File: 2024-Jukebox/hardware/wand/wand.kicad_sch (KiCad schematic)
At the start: 48 parts, among them J1 USB_C_Receptacle_USB2.0, J2 Conn_01x05, J3 Conn_01x04, J4 Conn_01x04, J5 Conn_01x04, J6 Conn_01x01, J7 Conn_01x04, Q1 MUN5214DW1T1G, Q2 BSS138, Q3 CJ3139K, Q5 BSS138, SW1 SW_SPDT, U1 CP2104, U2 ESP32-PICO-D4, U3 ICM-20948, U4 TP4065-4.2V, U5 MIC5225-3.3, U6 LY68L6400SLIT, U7 MIC5225-1.8

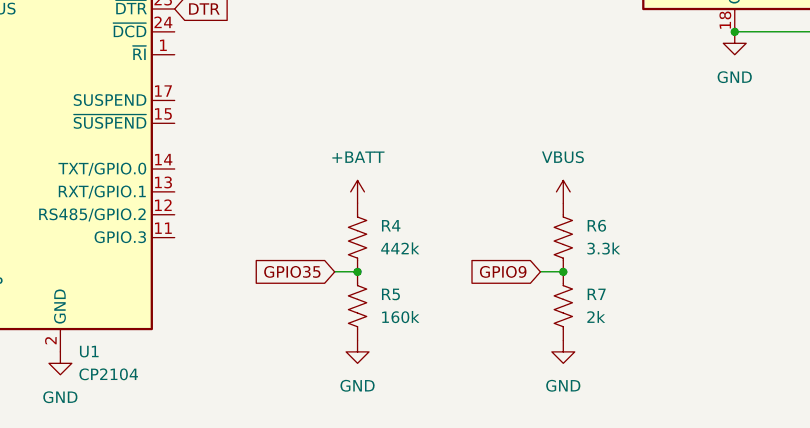
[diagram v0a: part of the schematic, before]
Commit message: Added wand production files
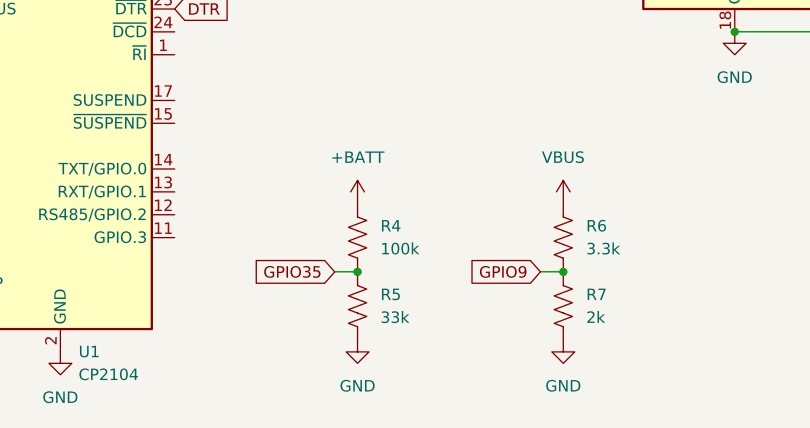
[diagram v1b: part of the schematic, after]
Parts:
- R4: value 442k -> 100k
- R5: value 160k -> 33k
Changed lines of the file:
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@@
       (effects (font (size 1.27 1.27)) (justify left))
     )
-    (property "Value" "160k" (at 125.73 180.34 0)
+    (property "Value" "33k" (at 125.73 180.34 0)
       (effects (font (size 1.27 1.27)) (justify left))
     )
@@
       (effects (font (size 1.27 1.27)) (justify left))
     )
-    (property "Value" "442k" (at 125.73 172.72 0)
-      (effects (font (size 1.27 1.27)) (justify left))
-    )
+    (property "Value" "100k" (at 125.73 172.72 0)
+      (effects (font (size 1.27 1.27)) (justify left))
+    )

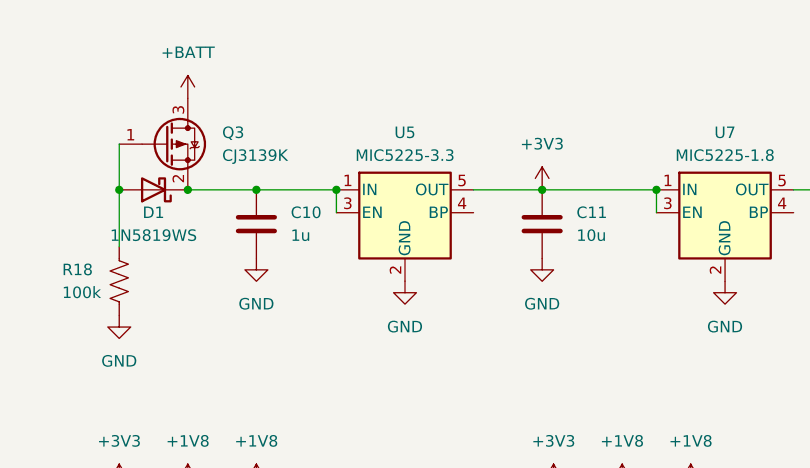
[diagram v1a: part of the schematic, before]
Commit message: Changed 3.3v regulator
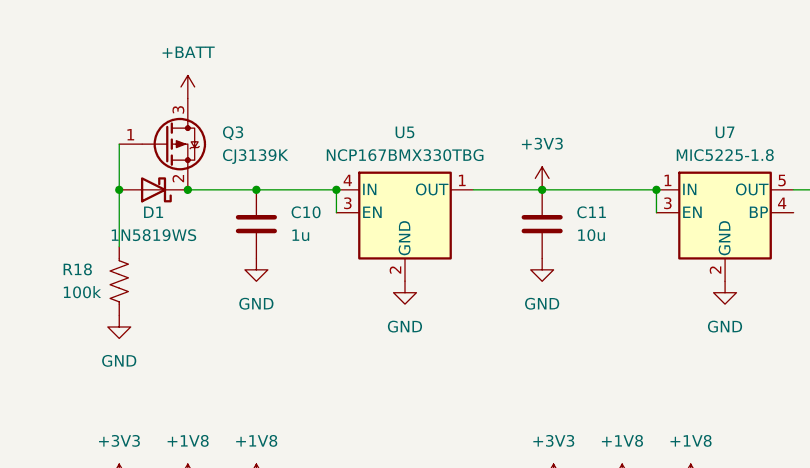
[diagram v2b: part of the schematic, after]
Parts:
- U5: value MIC5225-3.3 -> NCP167BMX330TBG; footprint Package_TO_SOT_SMD:SOT-23-5 -> Package_DFN_QFN:OnSemi_XDFN4-1EP_1.0x1.0mm_EP0.52x0.52mm
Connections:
- net +3V3: now also U5.1 (OUT); no longer U5.5 (OUT)
- net at C10.1, D1.1 (K), Q3.2 (S)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: now also U5.4 (IN); no longer U5.1 (IN)
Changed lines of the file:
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@@
     )
   )
-  (symbol (lib_id "Regulator_Linear:MIC5205-2.5YM5") (at 116.84 36.83 0) (unit 1)
+  (symbol (lib_name "MIC5205-2.5YM5_1") (lib_id "Regulator_Linear:MIC5205-2.5YM5") (at 116.84 36.83 0) (unit 1)
     (in_bom yes) (on_board yes) (dnp no) (fields_autoplaced)
     (property "Reference" "U5" (at 116.84 27.94 0)
       (effects (font (size 1.27 1.27)))
     )
-    (property "Value" "MIC5225-3.3" (at 116.84 30.48 0)
+    (property "Value" "NCP167BMX330TBG" (at 116.84 30.48 0)
       (effects (font (size 1.27 1.27)))
     )
-    (property "Footprint" "Package_TO_SOT_SMD:SOT-23-5" (at 116.84 28.575 0)
+    (property "Footprint" "Package_DFN_QFN:OnSemi_XDFN4-1EP_1.0x1.0mm_EP0.52x0.52mm" (at 116.84 28.575 0)
       (effects (font (size 1.27 1.27)) hide)
     )
@@
     (pin "3")
     (pin "4")
-    (pin "5")
     (instances
       (project "wand"
